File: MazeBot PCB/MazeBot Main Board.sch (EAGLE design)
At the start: 21 parts, among them IC1 7805TV, IC2 L298

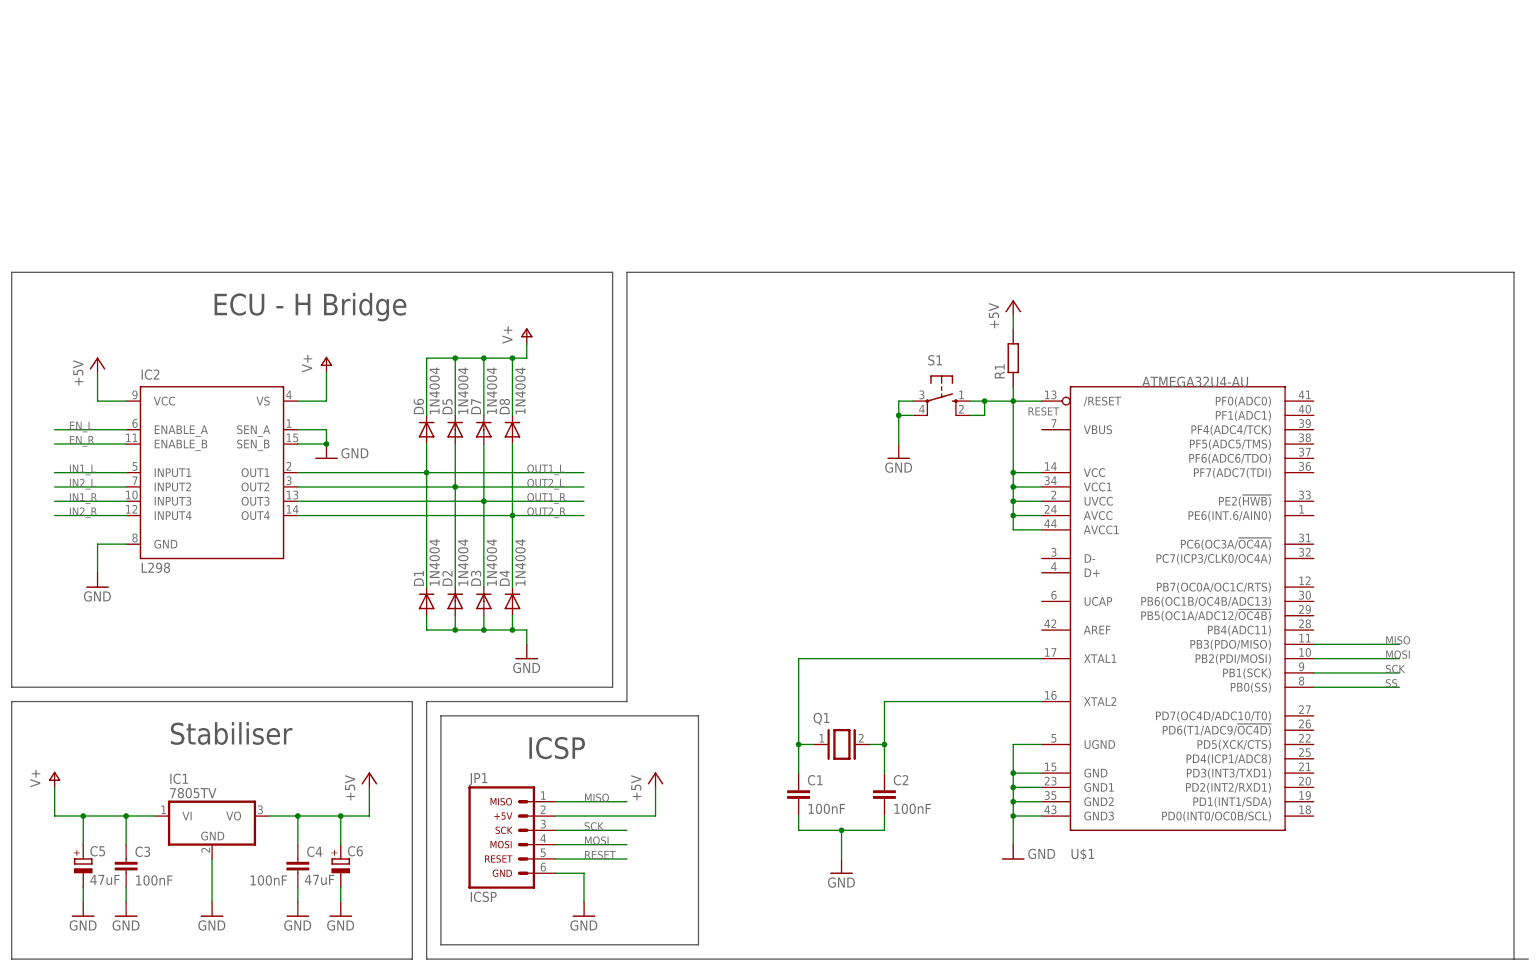
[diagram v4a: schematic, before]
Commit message: Add USB schematic
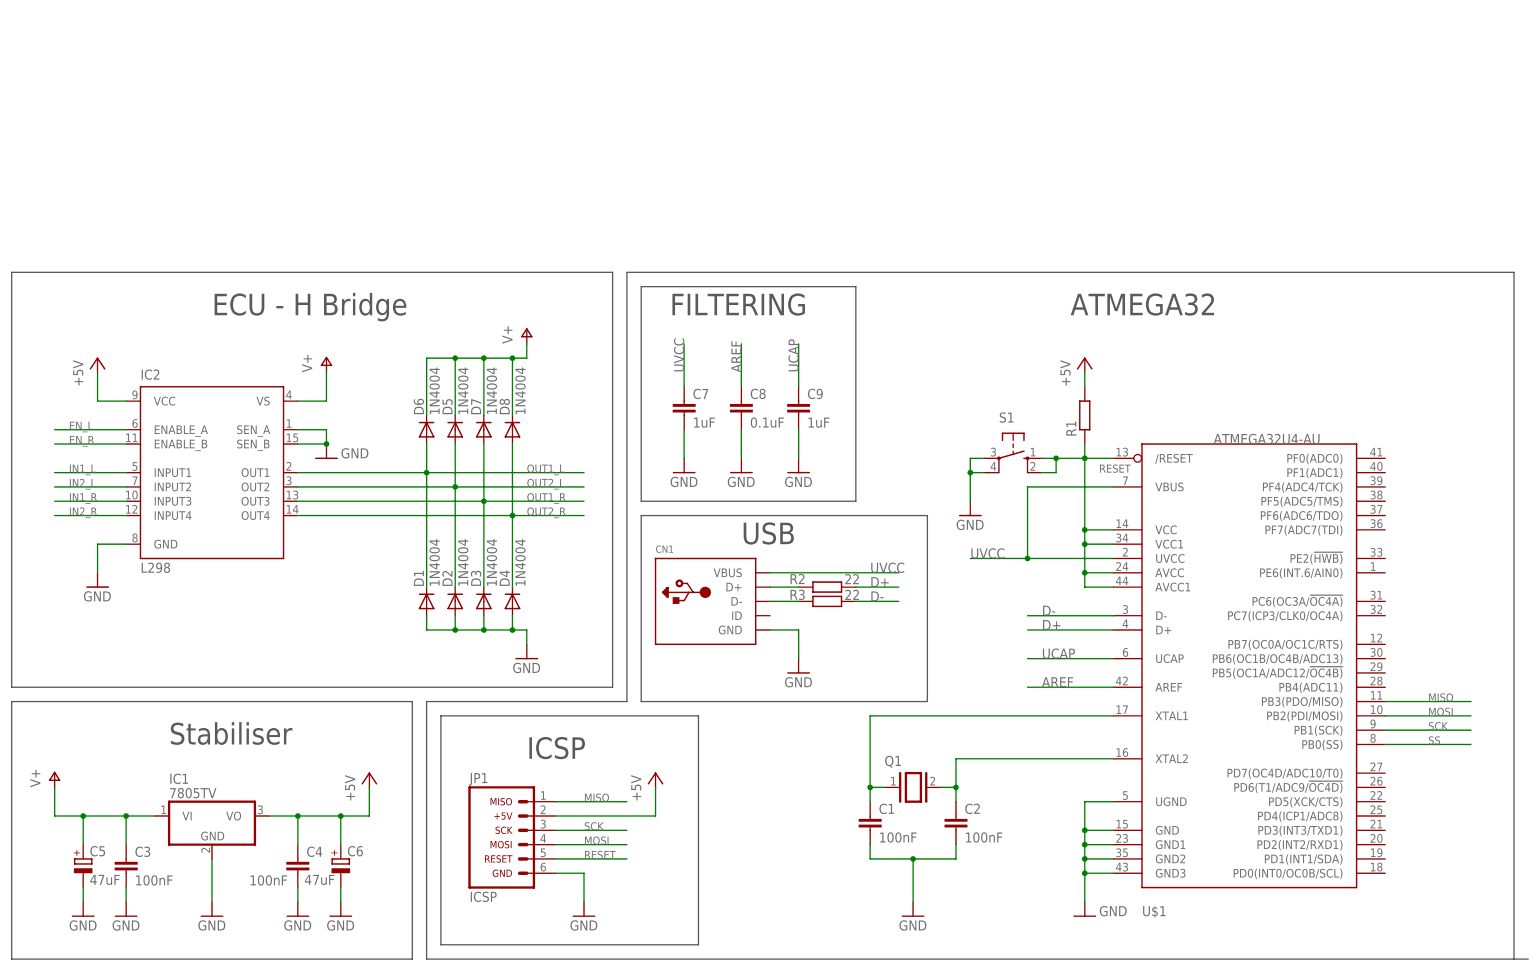
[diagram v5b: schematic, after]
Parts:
- added C7, C9: 1uF, rcl:C-EU025-024X044
- added C8: 0.1uF, rcl:C-EU025-024X044
- added CN1: (no value), adafruit:USBMINIB
- added R2, R3: 22, rcl:R-EU_0207/10
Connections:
- new net AREF: C8.1, U$1.AREF
- new net D+: R2.1, U$1.D+
- new net D-: R3.1, U$1.D-
- new net N$4: CN1.D+, R2.2
- new net N$5: CN1.D-, R3.2
- new net UCAP: C9.1, U$1.UCAP
- new net UVCC: C7.1, CN1.VBUS, U$1.UVCC, U$1.VBUS
- net GND: now also C7.2, C8.2, C9.2, CN1.GND
- net RESET: no longer U$1.UVCC
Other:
- note added: "ATMEGA32"
- note added: "FILTERING"
- note added: "USB"
- moved on the sheet: C1, C2, Q1, R1, S1, U$1

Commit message: Add signal routes
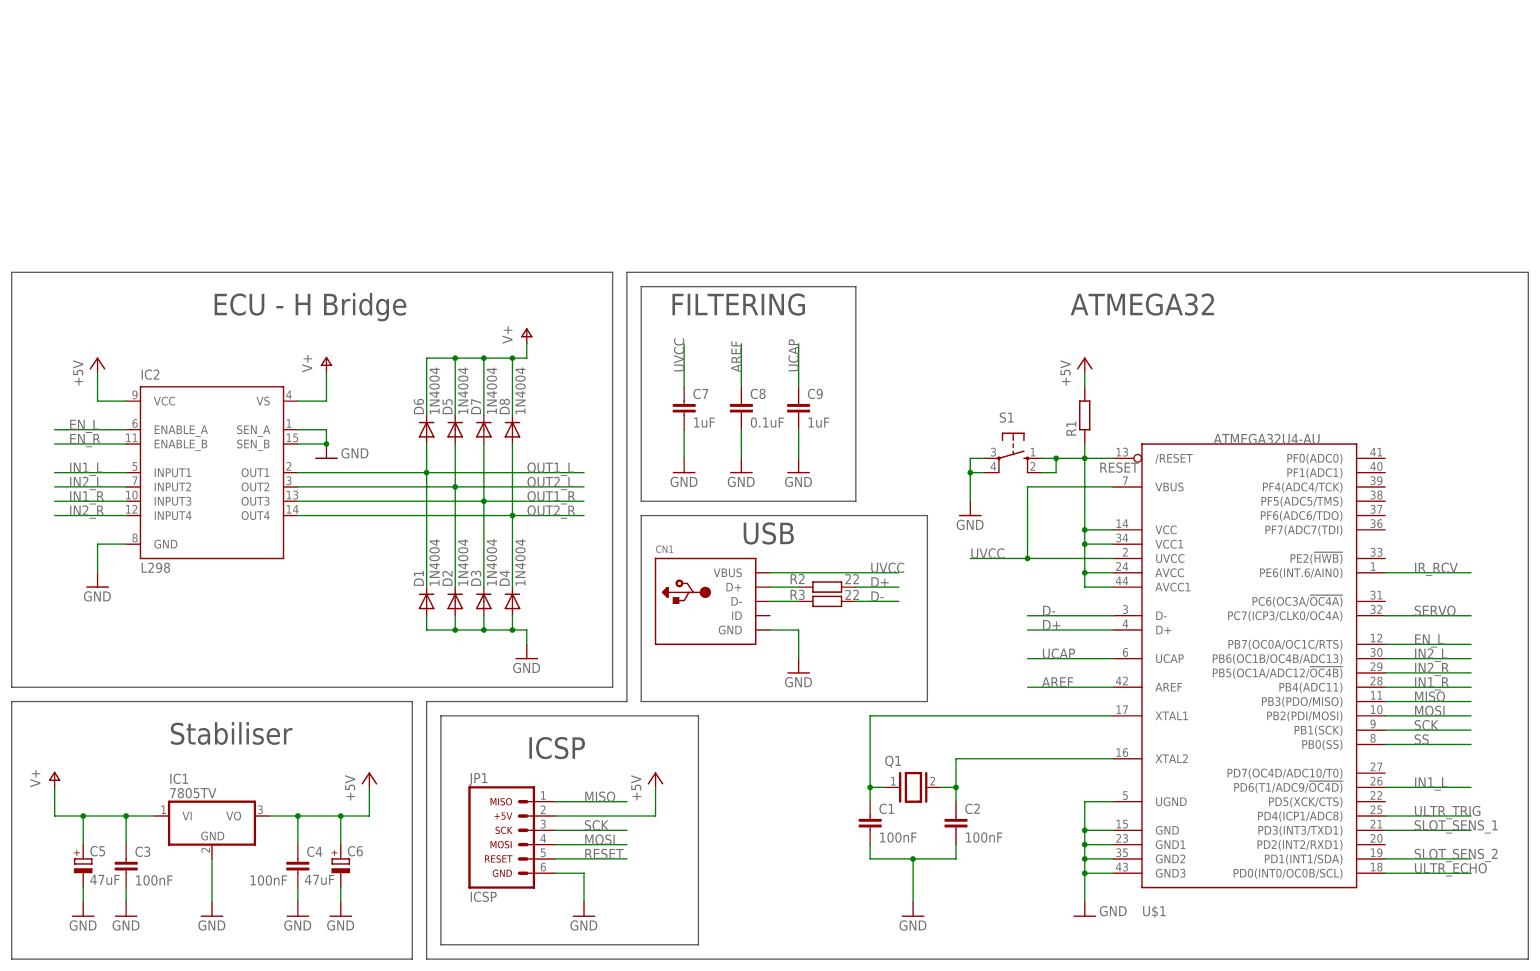
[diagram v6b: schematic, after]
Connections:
- new net IR_RCV: U$1.PE6(INT.6/AIN0)
- new net SERVO: U$1.PC7(ICP3/CLK0/OC4A)
- new net SLOT_SENS_1: U$1.PD3(INT3/TXD1)
- new net SLOT_SENS_2: U$1.PD1(INT1/SDA)
- new net ULTR_ECHO: U$1.PD0(INT0/OC0B/SCL)
- new net ULTR_TRIG: U$1.PD4(ICP1/ADC8)
- net EN_L: now also U$1.PB7(OC0A/OC1C/RTS)
- net IN1_L: now also U$1.PD6(T1/ADC9/!OC4D)
- net IN1_R: now also U$1.PB4(ADC11)
- net IN2_L: now also U$1.PB6(OC1B/OC4B/ADC13)
- net IN2_R: now also U$1.PB5(OC1A/ADC12/!OC4B)
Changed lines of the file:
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@@
 <setting verticaltext="up"/>
 </settings>
-<grid distance="0.1" unitdist="inch" unit="inch" style="dots" multiple="1" display="yes" altdistance="0.01" altunitdist="inch" altunit="inch"/>
+<grid distance="0.1" unitdist="inch" unit="inch" style="lines" multiple="1" display="no" altdistance="0.01" altunitdist="inch" altunit="inch"/>
 <layers>
 <layer number="1" name="Top" color="4" fill="1" visible="no" active="no"/>
@@
 <text x="96.52" y="40.64" size="3.81" layer="97">ICSP</text>
 <wire x1="78.74" y1="50.8" x2="78.74" y2="5.08" width="0.1524" layer="97"/>
-<wire x1="78.74" y1="5.08" x2="271.78" y2="5.08" width="0.1524" layer="97"/>
-<wire x1="274.32" y1="5.08" x2="271.78" y2="5.08" width="0.1524" layer="97"/>
-<wire x1="271.78" y1="5.08" x2="271.78" y2="127" width="0.1524" layer="97"/>
-<wire x1="271.78" y1="127" x2="114.3" y2="127" width="0.1524" layer="97"/>
+<wire x1="78.74" y1="5.08" x2="274.32" y2="5.08" width="0.1524" layer="97"/>
+<wire x1="274.32" y1="5.08" x2="274.32" y2="127" width="0.1524" layer="97"/>
+<wire x1="274.32" y1="127" x2="114.3" y2="127" width="0.1524" layer="97"/>
 <wire x1="114.3" y1="127" x2="114.3" y2="50.8" width="0.1524" layer="97"/>
 <wire x1="114.3" y1="50.8" x2="78.74" y2="50.8" width="0.1524" layer="97"/>
@@
 <pinref part="IC2" gate="L298" pin="ENABLE_A"/>
 <wire x1="25.4" y1="99.06" x2="12.7" y2="99.06" width="0.1524" layer="91"/>
-<label x="15.24" y="99.06" size="1.4224" layer="95"/>
+<label x="15.24" y="99.06" size="1.778" layer="95"/>
+</segment>
+<segment>
+<pinref part="U$1" gate="G$1" pin="PB7(OC0A/OC1C/RTS)"/>
+<wire x1="248.92" y1="60.96" x2="264.16" y2="60.96" width="0.1524" layer="91"/>
+<label x="254" y="60.96" size="1.778" layer="95"/>
 </segment>
 </net>
@@
 <pinref part="IC2" gate="L298" pin="ENABLE_B"/>
 <wire x1="25.4" y1="96.52" x2="12.7" y2="96.52" width="0.1524" layer="91"/>
-<label x="15.24" y="96.52" size="1.4224" layer="95"/>
+<label x="15.24" y="96.52" size="1.778" layer="95"/>
 </segment>
 </net>
@@
 <pinref part="IC2" gate="L298" pin="INPUT1"/>
 <wire x1="25.4" y1="91.44" x2="12.7" y2="91.44" width="0.1524" layer="91"/>
-<label x="15.24" y="91.44" size="1.4224" layer="95"/>
+<label x="15.24" y="91.44" size="1.778" layer="95"/>
+</segment>
+<segment>
+<pinref part="U$1" gate="G$1" pin="PD6(T1/ADC9/!OC4D)"/>
+<wire x1="248.92" y1="35.56" x2="264.16" y2="35.56" width="0.1524" layer="91"/>
+<label x="254" y="35.56" size="1.778" layer="95"/>
 </segment>
 </net>
@@
 <pinref part="IC2" gate="L298" pin="INPUT2"/>
 <wire x1="25.4" y1="88.9" x2="12.7" y2="88.9" width="0.1524" layer="91"/>
-<label x="15.24" y="88.9" size="1.4224" layer="95"/>
+<label x="15.24" y="88.9" size="1.778" layer="95"/>
+</segment>
+<segment>
+<pinref part="U$1" gate="G$1" pin="PB6(OC1B/OC4B/ADC13)"/>
+<wire x1="248.92" y1="58.42" x2="264.16" y2="58.42" width="0.1524" layer="91"/>
+<label x="254" y="58.42" size="1.778" layer="95"/>
 </segment>
 </net>
@@
 <pinref part="IC2" gate="L298" pin="INPUT3"/>
 <wire x1="25.4" y1="86.36" x2="12.7" y2="86.36" width="0.1524" layer="91"/>
-<label x="15.24" y="86.36" size="1.4224" layer="95"/>
+<label x="15.24" y="86.36" size="1.778" layer="95"/>
+</segment>
+<segment>
+<pinref part="U$1" gate="G$1" pin="PB4(ADC11)"/>
+<wire x1="248.92" y1="53.34" x2="264.16" y2="53.34" width="0.1524" layer="91"/>
+<label x="254" y="53.34" size="1.778" layer="95"/>
 </segment>
 </net>
@@
 <pinref part="IC2" gate="L298" pin="INPUT4"/>
 <wire x1="25.4" y1="83.82" x2="12.7" y2="83.82" width="0.1524" layer="91"/>
-<label x="15.24" y="83.82" size="1.4224" layer="95"/>
+<label x="15.24" y="83.82" size="1.778" layer="95"/>
+</segment>
+<segment>
+<pinref part="U$1" gate="G$1" pin="PB5(OC1A/ADC12/!OC4B)"/>
+<wire x1="248.92" y1="55.88" x2="264.16" y2="55.88" width="0.1524" layer="91"/>
+<label x="254" y="55.88" size="1.778" layer="95"/>
 </segment>
 </net>
@@
 <pinref part="D1" gate="1" pin="C"/>
 <wire x1="78.74" y1="91.44" x2="78.74" y2="71.12" width="0.1524" layer="91"/>
-<label x="96.52" y="91.44" size="1.4224" layer="95"/>
+<label x="96.52" y="91.44" size="1.778" layer="95"/>
 </segment>
 </net>
@@
 <pinref part="D2" gate="1" pin="C"/>
 <wire x1="83.82" y1="88.9" x2="83.82" y2="71.12" width="0.1524" layer="91"/>
-<label x="96.52" y="88.9" size="1.4224" layer="95"/>
+<label x="96.52" y="88.9" size="1.778" layer="95"/>
 </segment>
 </net>
@@
 <pinref part="D3" gate="1" pin="C"/>
 <wire x1="88.9" y1="86.36" x2="88.9" y2="71.12" width="0.1524" layer="91"/>
-<label x="96.52" y="86.36" size="1.4224" layer="95"/>
+<label x="96.52" y="86.36" size="1.778" layer="95"/>
 </segment>
 </net>
@@
 <pinref part="D4" gate="1" pin="C"/>
 <wire x1="93.98" y1="71.12" x2="93.98" y2="83.82" width="0.1524" layer="91"/>
-<label x="96.52" y="83.82" size="1.4224" layer="95"/>
+<label x="96.52" y="83.82" size="1.778" layer="95"/>
 <wire x1="93.98" y1="83.82" x2="106.68" y2="83.82" width="0.1524" layer="91"/>
 </segment>
@@
 <pinref part="U$1" gate="G$1" pin="PB1(SCK)"/>
 <wire x1="248.92" y1="45.72" x2="264.16" y2="45.72" width="0.1524" layer="91"/>
-<label x="256.54" y="45.72" size="1.4224" layer="95"/>
+<label x="254" y="45.72" size="1.778" layer="95"/>
 </segment>
 <segment>
 <pinref part="JP1" gate="G$1" pin="3"/>
 <wire x1="101.6" y1="27.94" x2="114.3" y2="27.94" width="0.1524" layer="91"/>
-<label x="106.68" y="27.94" size="1.4224" layer="95"/>
+<label x="106.68" y="27.94" size="1.778" layer="95"/>
 </segment>
 </net>
@@
 <pinref part="U$1" gate="G$1" pin="PB0(SS)"/>
 <wire x1="248.92" y1="43.18" x2="264.16" y2="43.18" width="0.1524" layer="91"/>
-<label x="256.54" y="43.18" size="1.4224" layer="95"/>
+<label x="254" y="43.18" size="1.778" layer="95"/>
 </segment>
 </net>
@@
 <pinref part="U$1" gate="G$1" pin="PB2(PDI/MOSI)"/>
 <wire x1="248.92" y1="48.26" x2="264.16" y2="48.26" width="0.1524" layer="91"/>
-<label x="256.54" y="48.26" size="1.4224" layer="95"/>
+<label x="254" y="48.26" size="1.778" layer="95"/>
 </segment>
 <segment>
 <pinref part="JP1" gate="G$1" pin="4"/>
 <wire x1="101.6" y1="25.4" x2="114.3" y2="25.4" width="0.1524" layer="91"/>
-<label x="106.68" y="25.4" size="1.4224" layer="95"/>
+<label x="106.68" y="25.4" size="1.778" layer="95"/>
 </segment>
 </net>
@@
 <pinref part="U$1" gate="G$1" pin="PB3(PDO/MISO)"/>
 <wire x1="248.92" y1="50.8" x2="264.16" y2="50.8" width="0.1524" layer="91"/>
-<label x="256.54" y="50.8" size="1.4224" layer="95"/>
+<label x="254" y="50.8" size="1.778" layer="95"/>
 </segment>
 <segment>
 <pinref part="JP1" gate="G$1" pin="1"/>
 <wire x1="101.6" y1="33.02" x2="114.3" y2="33.02" width="0.1524" layer="91"/>
-<label x="106.68" y="33.02" size="1.4224" layer="95"/>
+<label x="106.68" y="33.02" size="1.778" layer="95"/>
 </segment>
 </net>
@@
 <pinref part="R1" gate="G$1" pin="1"/>
 <wire x1="195.58" y1="96.52" x2="195.58" y2="93.98" width="0.1524" layer="91"/>
-<label x="198.12" y="91.44" size="1.4224" layer="95"/>
+<label x="198.12" y="91.44" size="1.778" layer="95"/>
 </segment>
 <segment>
 <pinref part="JP1" gate="G$1" pin="5"/>
 <wire x1="101.6" y1="22.86" x2="114.3" y2="22.86" width="0.1524" layer="91"/>
-<label x="106.68" y="22.86" size="1.4224" layer="95"/>
+<label x="106.68" y="22.86" size="1.778" layer="95"/>
 </segment>
 </net>
@@
 </segment>
 </net>
+<net name="SLOT_SENS_2" class="0">
+<segment>
+<pinref part="U$1" gate="G$1" pin="PD1(INT1/SDA)"/>
+<wire x1="248.92" y1="22.86" x2="264.16" y2="22.86" width="0.1524" layer="91"/>
+<label x="254" y="22.86" size="1.778" layer="95"/>
+</segment>
+</net>
+<net name="SLOT_SENS_1" class="0">
+<segment>
+<pinref part="U$1" gate="G$1" pin="PD3(INT3/TXD1)"/>
+<wire x1="248.92" y1="27.94" x2="264.16" y2="27.94" width="0.1524" layer="91"/>
+<label x="254" y="27.94" size="1.778" layer="95"/>
+</segment>
+</net>
+<net name="SERVO" class="0">
+<segment>
+<pinref part="U$1" gate="G$1" pin="PC7(ICP3/CLK0/OC4A)"/>
+<wire x1="248.92" y1="66.04" x2="264.16" y2="66.04" width="0.1524" layer="91"/>
+<label x="254" y="66.04" size="1.778" layer="95"/>
+</segment>
+</net>
+<net name="ULTR_TRIG" class="0">
+<segment>
+<pinref part="U$1" gate="G$1" pin="PD4(ICP1/ADC8)"/>
+<wire x1="248.92" y1="30.48" x2="264.16" y2="30.48" width="0.1524" layer="91"/>
+<label x="254" y="30.48" size="1.778" layer="95"/>
+</segment>
+</net>
+<net name="ULTR_ECHO" class="0">
+<segment>
+<pinref part="U$1" gate="G$1" pin="PD0(INT0/OC0B/SCL)"/>
+<wire x1="248.92" y1="20.32" x2="264.16" y2="20.32" width="0.1524" layer="91"/>
+<label x="254" y="20.32" size="1.778" layer="95"/>
+</segment>
+</net>
+<net name="IR_RCV" class="0">
+<segment>
+<pinref part="U$1" gate="G$1" pin="PE6(INT.6/AIN0)"/>
+<wire x1="248.92" y1="73.66" x2="264.16" y2="73.66" width="0.1524" layer="91"/>
+<label x="254" y="73.66" size="1.778" layer="95"/>
+</segment>
+</net>

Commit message: Move inside a frame
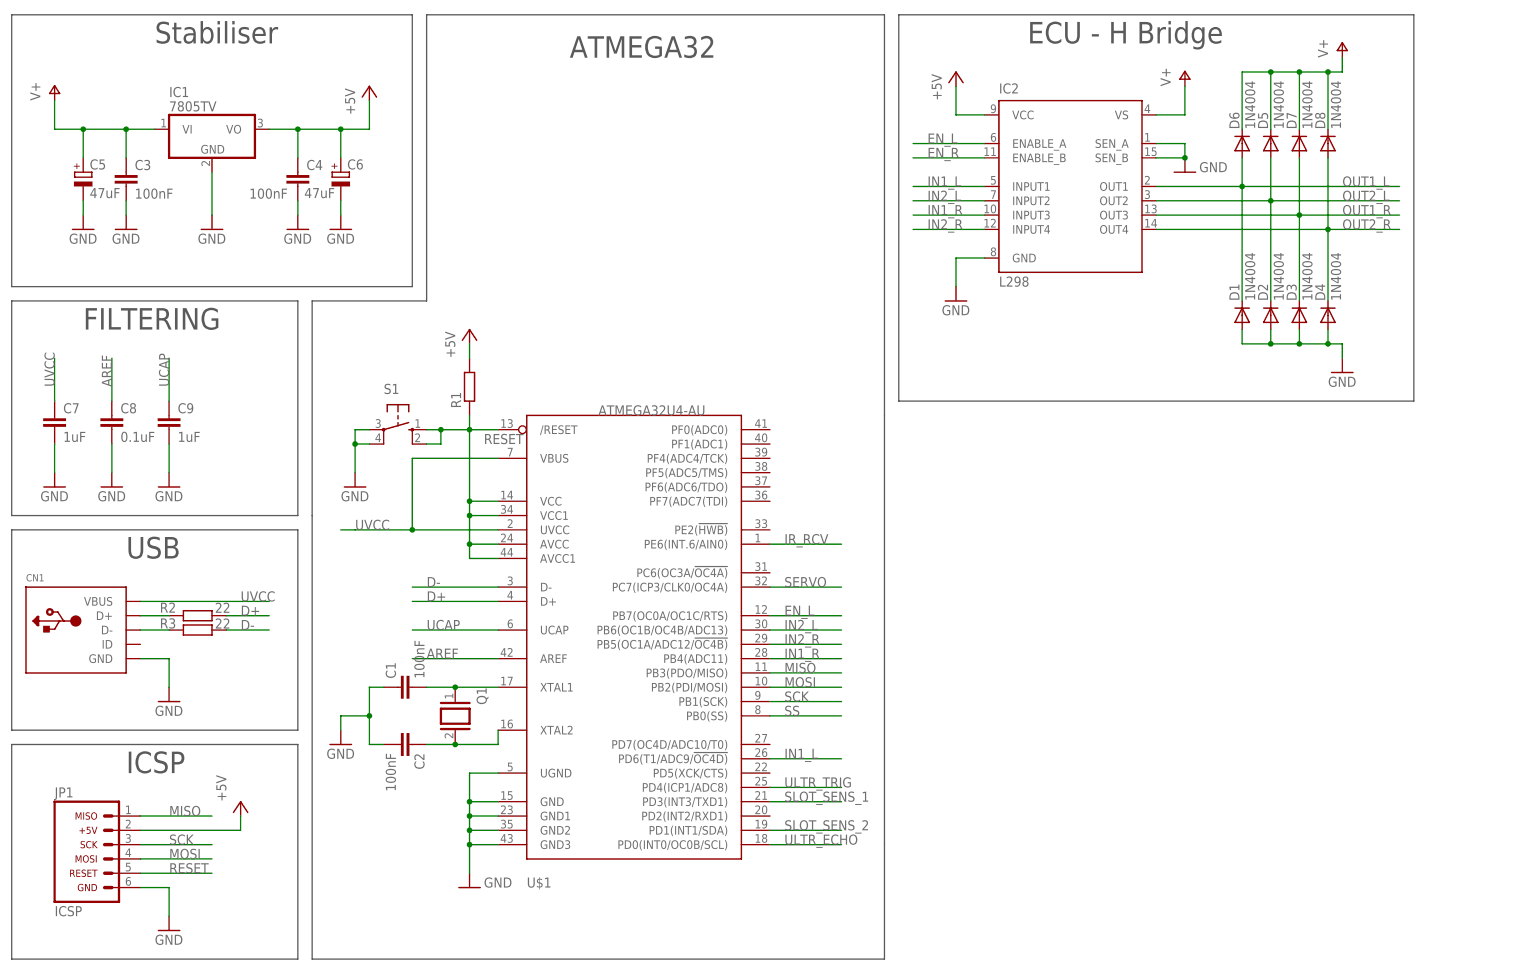
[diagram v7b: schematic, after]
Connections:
- net GND: now also C1.1; no longer C1.2
- net N$1: now also C1.2; no longer C1.1
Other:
- moved on the sheet: C1, C2, C3, C4, C5, C6, C7, C8, C9, CN1, D1, D2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
